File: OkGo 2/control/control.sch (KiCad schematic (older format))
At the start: 51 parts, among them P101 KEYSW, P102 KEYSW, P103 BATT_CASE, P104 BATT, P105 BATT, P106 ARM_LED, P107 ARM_LED, P108 SMA, P109 POWER_SW, P110 POWER_SW, SW101 KEYSWITCH, SW102 LATCHING PUSH, U101 SWD, U102 STM32F071CBT6, U103 MEJ2S0305SC, U104 BEZEL, U105 RFM95W, U106 LCD_HD44780, U107 ADP3335, Y101 8MHz

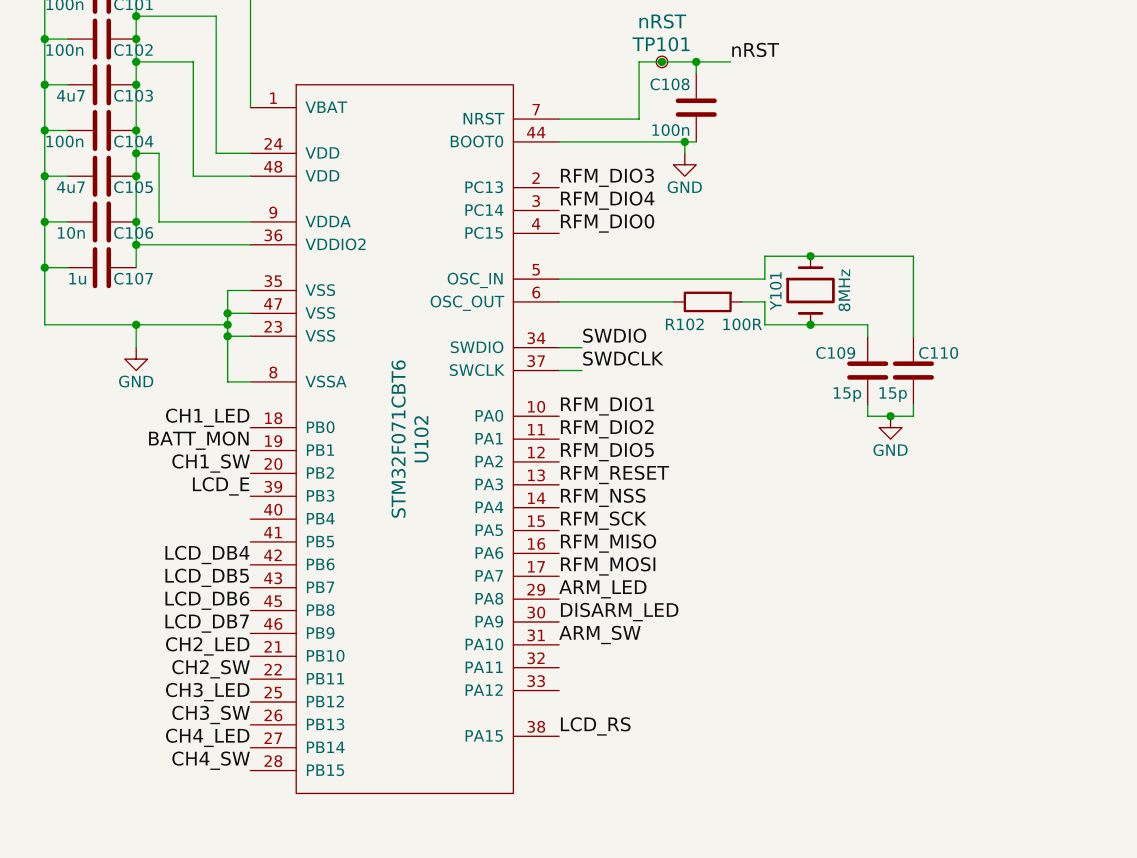
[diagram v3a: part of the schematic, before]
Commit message: Added serial interface, resolves #19
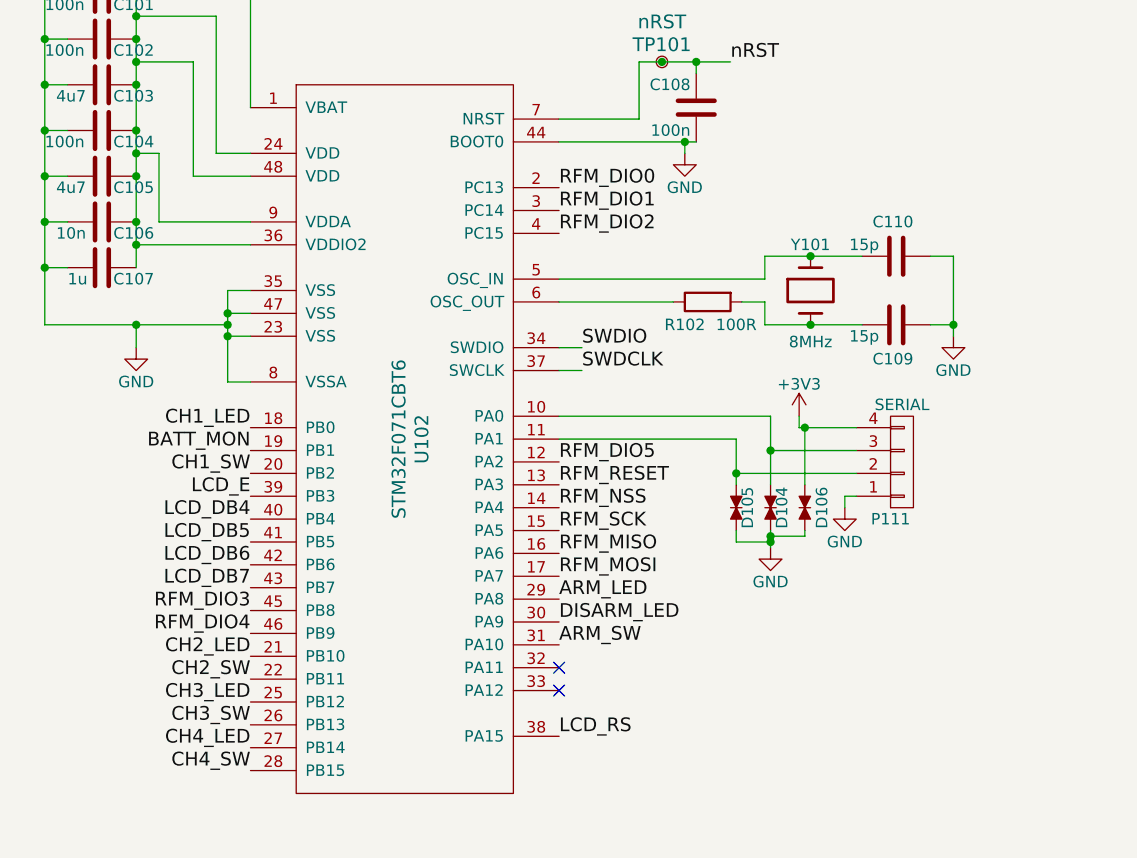
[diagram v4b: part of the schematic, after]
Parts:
- added D104, D105, D106: TVS_small, Resistors_SMD:R_0603, symbol TVS_small
- added P111: SERIAL, common:JST-PA-4, symbol CONN_01X04
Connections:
- net +3V3: now also D106.1, P111.4 (P4)
- net GND: now also D104.2, D105.2, D106.2, P111.1 (P1)
- net LCD_DB4: now also U102.40 (PB4); no longer U102.42 (PB6)
- net LCD_DB5: now also U102.41 (PB5); no longer U102.43 (PB7)
- net LCD_DB6: now also U102.42 (PB6); no longer U102.45 (PB8)
- net LCD_DB7: now also U102.43 (PB7); no longer U102.46 (PB9)
- net RFM_DIO0: now also U102.2 (PC13); no longer U102.4 (PC15)
- net RFM_DIO1: now also U102.3 (PC14); no longer U102.10 (PA0)
- net RFM_DIO2: now also U102.4 (PC15); no longer U102.11 (PA1)
- net RFM_DIO3: now also U102.45 (PB8); no longer U102.2 (PC13)
- net RFM_DIO4: now also U102.46 (PB9); no longer U102.3 (PC14)
- new net: D104.1, P111.3 (P3), U102.10 (PA0)
- new net: D105.1, P111.2 (P2), U102.11 (PA1)
- no-connect marks 2 -> 4
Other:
- moved on the sheet: C109, C110

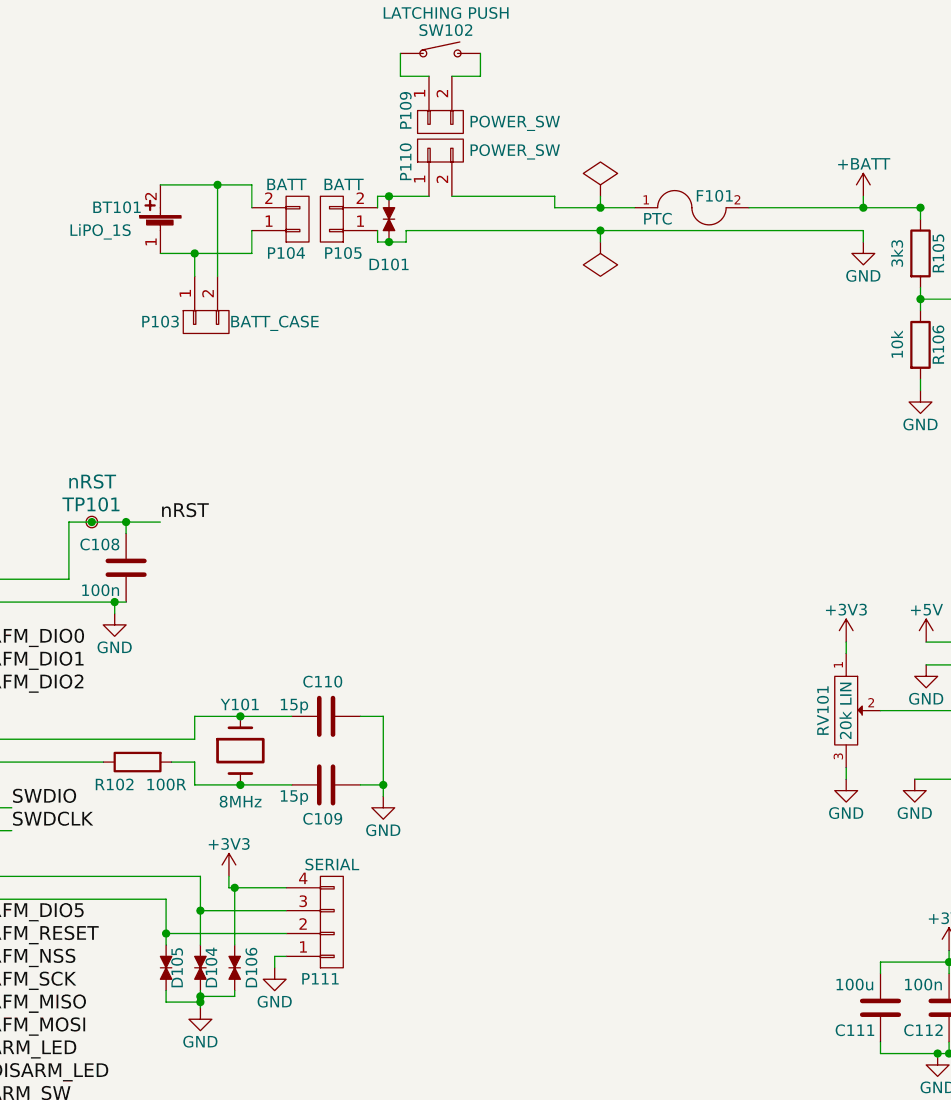
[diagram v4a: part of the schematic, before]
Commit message: 2nd route of control, sans cleaning and checking
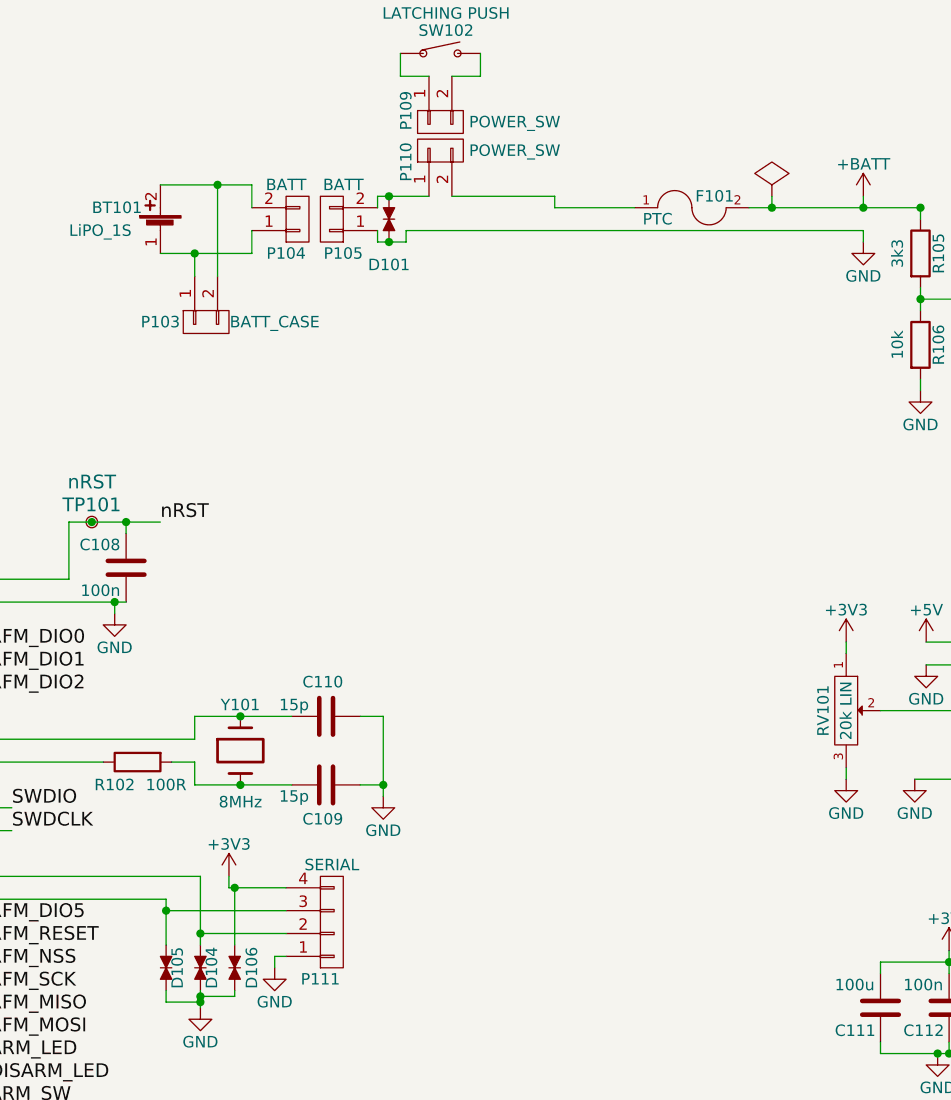
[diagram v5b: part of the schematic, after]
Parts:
- R106: footprint Capacitors_SMD:C_0805 -> Resistors_SMD:R_0805
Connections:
- net at D104.1, U102.10 (PA0): now also P111.2 (P2); no longer P111.3 (P3)
- net at D105.1, U102.11 (PA1): now also P111.3 (P3); no longer P111.2 (P2)
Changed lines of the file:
@@
 L PWR_FLAG #FLG06
 U 1 1 556217FC
-P 5725 1600
-F 0 "#FLG06" H 5725 1695 50  0001 C CNN
-F 1 "PWR_FLAG" H 5725 1780 50  0001 C CNN
-F 2 "" H 5725 1600 60  0000 C CNN
-F 3 "" H 5725 1600 60  0000 C CNN
-	1    5725 1600
-	1    0    0    -1
-$EndComp
-$Comp
-L PWR_FLAG #FLG07
-U 1 1 55621881
-P 5725 1800
-F 0 "#FLG07" H 5725 1895 50  0001 C CNN
-F 1 "PWR_FLAG" H 5725 1980 50  0001 C CNN
-F 2 "" H 5725 1800 60  0000 C CNN
-F 3 "" H 5725 1800 60  0000 C CNN
-	1    5725 1800
-	-1   0    0    1
-$EndComp
-$Comp
-L GND #PWR08
+P 6475 1600
+F 0 "#FLG06" H 6475 1695 50  0001 C CNN
+F 1 "PWR_FLAG" H 6475 1780 50  0001 C CNN
+F 2 "" H 6475 1600 60  0000 C CNN
+F 3 "" H 6475 1600 60  0000 C CNN
+	1    6475 1600
+	1    0    0    -1
+$EndComp
+$Comp
+L GND #PWR07
 U 1 1 55629E65
 P 9000 6300
-F 0 "#PWR08" H 9000 6050 50  0001 C CNN
+F 0 "#PWR07" H 9000 6050 50  0001 C CNN
 F 1 "GND" H 9000 6150 50  0001 C CNN
 F 2 "" H 9000 6300 60  0000 C CNN
@@
 $EndComp
 $Comp
-L GND #PWR09
+L GND #PWR08
 U 1 1 5562B214
 P 7200 5350
-F 0 "#PWR09" H 7200 5100 50  0001 C CNN
+F 0 "#PWR08" H 7200 5100 50  0001 C CNN
 F 1 "GND" H 7200 5200 50  0000 C CNN
 F 2 "" H 7200 5350 60  0000 C CNN
@@
 $EndComp
 $Comp
-L +3V3 #PWR010
+L +3V3 #PWR09
 U 1 1 5562B35A
 P 7250 4900
-F 0 "#PWR010" H 7250 4750 50  0001 C CNN
+F 0 "#PWR09" H 7250 4750 50  0001 C CNN
 F 1 "+3V3" H 7250 5040 50  0000 C CNN
 F 2 "" H 7250 4900 60  0000 C CNN
@@
 $EndComp
 $Comp
-L +3V3 #PWR011
+L +3V3 #PWR010
 U 1 1 55624CAA
 P 10650 850
-F 0 "#PWR011" H 10650 700 50  0001 C CNN
+F 0 "#PWR010" H 10650 700 50  0001 C CNN
 F 1 "+3V3" H 10650 990 50  0000 C CNN
 F 2 "" H 10650 850 60  0000 C CNN
@@
 $EndComp
 $Comp
-L +3V3 #PWR012
+L +3V3 #PWR011
 U 1 1 5562C6B7
 P 1200 2575
-F 0 "#PWR012" H 1200 2425 50  0001 C CNN
+F 0 "#PWR011" H 1200 2425 50  0001 C CNN
 F 1 "+3V3" H 1200 2715 50  0000 C CNN
 F 2 "" H 1200 2575 60  0000 C CNN
@@
 $EndComp
 $Comp
-L GND #PWR013
+L GND #PWR012
 U 1 1 5562DCAE
 P 1200 4275
-F 0 "#PWR013" H 1200 4025 50  0001 C CNN
+F 0 "#PWR012" H 1200 4025 50  0001 C CNN
 F 1 "GND" H 1200 4125 50  0000 C CNN
 F 2 "" H 1200 4275 60  0000 C CNN
@@
 $EndComp
 $Comp
-L GND #PWR014
+L GND #PWR013
 U 1 1 5562E73A
 P 3600 3425
-F 0 "#PWR014" H 3600 3175 50  0001 C CNN
+F 0 "#PWR013" H 3600 3175 50  0001 C CNN
 F 1 "GND" H 3600 3275 50  0000 C CNN
 F 2 "" H 3600 3425 60  0000 C CNN
@@
 $EndComp
 $Comp
-L +3V3 #PWR015
+L +3V3 #PWR014
 U 1 1 556484DA
 P 925 6750
-F 0 "#PWR015" H 925 6600 50  0001 C CNN
+F 0 "#PWR014" H 925 6600 50  0001 C CNN
 F 1 "+3V3" H 925 6890 50  0000 C CNN
 F 2 "" H 925 6750 60  0000 C CNN
@@
 $EndComp
 $Comp
-L GND #PWR016
+L GND #PWR015
 U 1 1 5564860C
 P 875 7250
-F 0 "#PWR016" H 875 7000 50  0001 C CNN
+F 0 "#PWR015" H 875 7000 50  0001 C CNN
 F 1 "GND" H 875 7100 50  0000 C CNN
 F 2 "" H 875 7250 60  0000 C CNN
@@
 F 0 "R106" V 7205 2250 50  0000 C CNN
 F 1 "10k" V 7025 2250 50  0000 C CNN
-F 2 "Capacitors_SMD:C_0805" V 7055 2250 30  0001 C CNN
+F 2 "Resistors_SMD:R_0805" V 7055 2250 30  0001 C CNN
 F 3 "" H 7125 2250 30  0000 C CNN
 F 4 "9237755" H 7125 2250 60  0001 C CNN "Farnell"
@@
 $EndComp
 $Comp
-L GND #PWR017
+L GND #PWR016
 U 1 1 556523AF
 P 7125 2450
-F 0 "#PWR017" H 7125 2200 50  0001 C CNN
+F 0 "#PWR016" H 7125 2200 50  0001 C CNN
 F 1 "GND" H 7125 2300 50  0000 C CNN
 F 2 "" H 7125 2450 60  0000 C CNN
@@
 $EndComp
 $Comp
-L +3V3 #PWR018
+L +3V3 #PWR017
 U 1 1 5563E071
 P 7500 3250
-F 0 "#PWR018" H 7500 3100 50  0001 C CNN
+F 0 "#PWR017" H 7500 3100 50  0001 C CNN
 F 1 "+3V3" H 7500 3390 50  0000 C CNN
 F 2 "" H 7500 3250 60  0000 C CNN
@@
 $EndComp
 $Comp
-L GND #PWR019
+L GND #PWR018
 U 1 1 5563E174
 P 7500 3350
-F 0 "#PWR019" H 7500 3100 50  0001 C CNN
+F 0 "#PWR018" H 7500 3100 50  0001 C CNN
 F 1 "GND" H 7500 3200 50  0000 C CNN
 F 2 "" H 7500 3350 60  0000 C CNN
@@
 $EndComp
 $Comp
-L +3V3 #PWR020
+L +3V3 #PWR019
 U 1 1 5563E7A7
 P 6800 3550
-F 0 "#PWR020" H 6800 3400 50  0001 C CNN
+F 0 "#PWR019" H 6800 3400 50  0001 C CNN
 F 1 "+3V3" H 6800 3690 50  0000 C CNN
 F 2 "" H 6800 3550 60  0000 C CNN
@@
 $EndComp
 $Comp
-L GND #PWR021
+L GND #PWR020
 U 1 1 5563E8D6
 P 6800 4150
-F 0 "#PWR021" H 6800 3900 50  0001 C CNN
+F 0 "#PWR020" H 6800 3900 50  0001 C CNN
 F 1 "GND" H 6800 4000 50  0000 C CNN
 F 2 "" H 6800 4150 60  0000 C CNN
@@
 $EndComp
 $Comp
-L GND #PWR022
+L GND #PWR021
 U 1 1 55643E77
 P 7150 3650
-F 0 "#PWR022" H 7150 3400 50  0001 C CNN
+F 0 "#PWR021" H 7150 3400 50  0001 C CNN
 F 1 "GND" H 7150 3500 50  0000 C CNN
 F 2 "" H 7150 3650 60  0000 C CNN
@@
 $EndComp
 $Comp
-L GND #PWR023
+L GND #PWR022
 U 1 1 55638AFF
 P 7100 4150
-F 0 "#PWR023" H 7100 3900 50  0001 C CNN
+F 0 "#PWR022" H 7100 3900 50  0001 C CNN
 F 1 "GND" H 7100 4000 50  0000 C CNN
 F 2 "" H 7100 4150 60  0000 C CNN
@@
 $EndComp
 $Comp
-L GND #PWR024
+L GND #PWR023
 U 1 1 559E503C
 P 9000 5850
-F 0 "#PWR024" H 9000 5600 50  0001 C CNN
+F 0 "#PWR023" H 9000 5600 50  0001 C CNN
 F 1 "GND" H 9000 5700 50  0001 C CNN
 F 2 "" H 9000 5850 60  0000 C CNN
@@
 $EndComp
 $Comp
-L +3V3 #PWR025
+L +3V3 #PWR024
 U 1 1 559EA6BB
 P 3150 7050
-F 0 "#PWR025" H 3150 6900 50  0001 C CNN
+F 0 "#PWR024" H 3150 6900 50  0001 C CNN
 F 1 "+3V3" H 3150 7190 50  0000 C CNN
 F 2 "" H 3150 7050 60  0000 C CNN
@@
 $EndComp
 $Comp
-L GND #PWR026
+L GND #PWR025
 U 1 1 559EA828
 P 3150 7250
-F 0 "#PWR026" H 3150 7000 50  0001 C CNN
+F 0 "#PWR025" H 3150 7000 50  0001 C CNN
 F 1 "GND" H 3150 7100 50  0000 C CNN
 F 2 "" H 3150 7250 60  0000 C CNN
@@
 $EndComp
 $Comp
-L +5V #PWR027
+L +5V #PWR026
 U 1 1 559EAA6F
 P 4350 7050
-F 0 "#PWR027" H 4350 6900 50  0001 C CNN
+F 0 "#PWR026" H 4350 6900 50  0001 C CNN
 F 1 "+5V" H 4350 7190 50  0000 C CNN
 F 2 "" H 4350 7050 60  0000 C CNN
@@
 $EndComp
 $Comp
-L GND #PWR028
+L GND #PWR027
 U 1 1 559EABE0
 P 4350 7250
-F 0 "#PWR028" H 4350 7000 50  0001 C CNN
+F 0 "#PWR027" H 4350 7000 50  0001 C CNN
 F 1 "GND" H 4350 7100 50  0000 C CNN
 F 2 "" H 4350 7250 60  0000 C CNN
@@
 $EndComp
 $Comp
-L +BATT #PWR029
+L +BATT #PWR028
 U 1 1 55A7EBCE
 P 8300 900
-F 0 "#PWR029" H 8300 750 50  0001 C CNN
+F 0 "#PWR028" H 8300 750 50  0001 C CNN
 F 1 "+BATT" H 8300 1040 50  0000 C CNN
 F 2 "" H 8300 900 60  0000 C CNN
@@
 $EndComp
 $Comp
-L GND #PWR030
+L GND #PWR029
 U 1 1 55A805A4
 P 10275 2750
-F 0 "#PWR030" H 10275 2500 50  0001 C CNN
+F 0 "#PWR029" H 10275 2500 50  0001 C CNN
 F 1 "GND" H 10275 2600 50  0000 C CNN
 F 2 "" H 10275 2750 60  0000 C CNN
@@
 $EndComp
 $Comp
-L +3.3V #PWR031
+L +3.3V #PWR030
 U 1 1 55A80891
 P 10325 2200
-F 0 "#PWR031" H 10325 2050 50  0001 C CNN
+F 0 "#PWR030" H 10325 2050 50  0001 C CNN
 F 1 "+3.3V" H 10325 2340 50  0000 C CNN
 F 2 "" H 10325 2200 60  0000 C CNN
@@
 GREEN: 2.1V 20mA
 $Comp
-L +5V #PWR032
+L +5V #PWR031
 U 1 1 55AC453D
 P 7150 3550
-F 0 "#PWR032" H 7150 3400 50  0001 C CNN
+F 0 "#PWR031" H 7150 3400 50  0001 C CNN
 F 1 "+5V" H 7150 3690 50  0000 C CNN
 F 2 "" H 7150 3550 60  0000 C CNN
@@
 $EndComp
 $Comp
-L GND #PWR033
+L GND #PWR032
 U 1 1 55B80248
 P 9400 4150
-F 0 "#PWR033" H 9400 3900 50  0001 C CNN
+F 0 "#PWR032" H 9400 3900 50  0001 C CNN
 F 1 "GND" H 9400 4000 50  0000 C CNN
 F 2 "" H 9400 4150 60  0000 C CNN
@@
 $EndComp
 $Comp
-L GND #PWR034
+L GND #PWR033
 U 1 1 55BA3B3F
 P 4775 4225
-F 0 "#PWR034" H 4775 3975 50  0001 C CNN
+F 0 "#PWR033" H 4775 3975 50  0001 C CNN
 F 1 "GND" H 4775 4075 50  0000 C CNN
 F 2 "" H 4775 4225 60  0000 C CNN
@@
 $EndComp
 $Comp
-L GND #PWR035
+L GND #PWR034
 U 1 1 55BA4EAC
 P 4300 4975
-F 0 "#PWR035" H 4300 4725 50  0001 C CNN
+F 0 "#PWR034" H 4300 4725 50  0001 C CNN
 F 1 "GND" H 4300 4825 50  0000 C CNN
 F 2 "" H 4300 4975 60  0000 C CNN
@@
 	4875 1750 6875 1750
 Wire Wire Line
-	5725 1600 5725 1650
-Connection ~ 5725 1650
-Wire Wire Line
-	5725 1800 5725 1750
-Connection ~ 5725 1750
-Wire Wire Line
 	6875 1650 6875 1600
 Wire Wire Line
@@
 	3050 4575 3975 4575
 $Comp
-L +3V3 #PWR036
+L +3V3 #PWR035
 U 1 1 55BB5B12
 P 4100 4575
-F 0 "#PWR036" H 4100 4425 50  0001 C CNN
+F 0 "#PWR035" H 4100 4425 50  0001 C CNN
 F 1 "+3V3" H 4100 4715 50  0000 C CNN
 F 2 "" H 4100 4575 60  0000 C CNN
@@
 	4300 4925 4300 4975
 Wire Wire Line
-	3975 4725 4350 4725
-Wire Wire Line
-	3825 4825 4350 4825
-Wire Wire Line
 	3975 4575 3975 4875
-Wire Wire Line
-	3825 4675 3825 4875
 Wire Wire Line
 	3825 4675 3050 4675
@@
 	4125 4625 4125 4875
 Connection ~ 4125 4625
-Connection ~ 3975 4725
-Connection ~ 3825 4825
-$Comp
-L GND #PWR037
+$Comp
+L GND #PWR036
 U 1 1 55BBFDE6
 P 3975 5150
-F 0 "#PWR037" H 3975 4900 50  0001 C CNN
+F 0 "#PWR036" H 3975 4900 50  0001 C CNN
 F 1 "GND" H 3975 5000 50  0000 C CNN
 F 2 "" H 3975 5150 60  0000 C CNN
@@
 NoConn ~ 3050 5675
 NoConn ~ 3050 5775
+Wire Wire Line
+	6475 1600 6475 1650
+Connection ~ 6475 1650
+Wire Wire Line
+	3825 4675 3825 4875
+Wire Wire Line
+	4350 4725 3825 4725
+Connection ~ 3825 4725
+Wire Wire Line
+	4350 4825 3975 4825
+Connection ~ 3975 4825
 $EndSCHEMATC

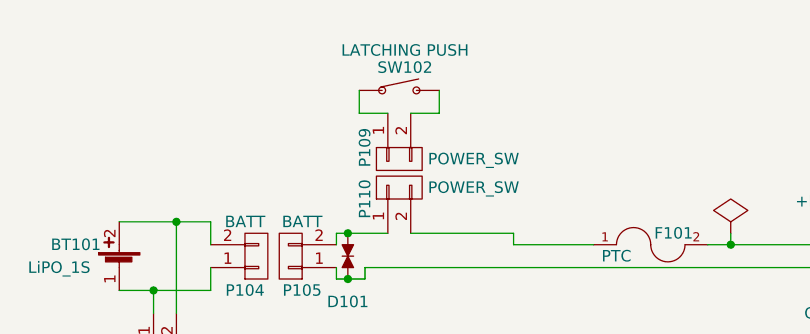
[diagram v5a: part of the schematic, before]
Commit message: Footprinting, rockers
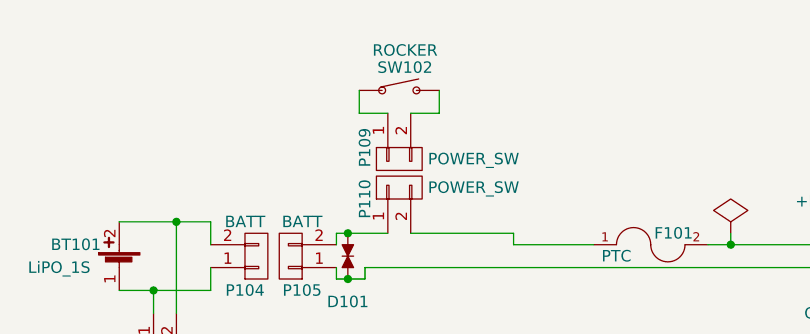
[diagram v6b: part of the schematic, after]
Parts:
- SW102: value LATCHING PUSH -> ROCKER; Farnell SW02719 -> 1839503
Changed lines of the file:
@@
 P 5050 975
 F 0 "SW102" H 5050 1075 50  0000 C CNN
-F 1 "LATCHING PUSH" H 5050 1150 50  0000 C CNN
+F 1 "ROCKER" H 5050 1150 50  0000 C CNN
 F 2 "" H 5050 975 60  0000 C CNN
-F 3 "" H 5050 975 60  0000 C CNN
-F 4 "SW02719" H 5050 975 60  0001 C CNN "Farnell"
+F 3 "http://www.farnell.com/datasheets/624901.pdf" H 5050 975 60  0001 C CNN
+F 4 "1839503" H 5050 975 60  0001 C CNN "Farnell"
 	1    5050 975
 	1    0    0    -1

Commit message: Changed SMA-F part
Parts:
- P108: Farnell 1608592 -> 1342651
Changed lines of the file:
@@
 F 2 "common:SMA-142-0701-801" H 9150 6050 60  0001 C CNN
 F 3 "" H 9150 6050 60  0000 C CNN
-F 4 "1608592" H 9150 6050 60  0001 C CNN "Farnell"
+F 4 "1342651" H 9150 6050 60  0001 C CNN "Farnell"
 	1    9150 6050
 	1    0    0    -1

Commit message: Corrected a bunch of footprints, see #9
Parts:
- F101: footprint Resistors_SMD:R_0805 -> control:polyfuse0805
- U102: footprint Housings_QFP:LQFP-48_7x7mm_Pitch0.5mm -> common:LQFP48_ST
- U107: footprint Housings_SSOP:MSOP-8_3x3mm_Pitch0.65mm -> control:MSOP-8_3x3mm_Pitch0.65mm
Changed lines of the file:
@@
 F 0 "U102" V 2450 4975 60  0000 C CNN
 F 1 "STM32F071CBT6" V 2350 4975 60  0000 C CNN
-F 2 "Housings_QFP:LQFP-48_7x7mm_Pitch0.5mm" H 2400 5025 60  0001 C CNN
+F 2 "common:LQFP48_ST" H 2400 5025 60  0001 C CNN
 F 3 "http://www.st.com/st-web-ui/static/active/en/resource/technical/document/datasheet/DM00098745.pdf" H 2400 5025 60  0001 C CNN
 F 4 "2432093" H 2400 4825 60  0001 C CNN "Farnell"
@@
 F 0 "U107" V 9500 950 60  0000 C CNN
 F 1 "ADP3335" V 9400 950 60  0000 C CNN
-F 2 "Housings_SSOP:MSOP-8_3x3mm_Pitch0.65mm" H 9400 1100 60  0001 C CNN
+F 2 "control:MSOP-8_3x3mm_Pitch0.65mm" H 9400 1100 60  0001 C CNN
 F 3 "" H 9400 1100 60  0000 C CNN
 F 4 "2067775" H 9400 950 60  0001 C CNN "Farnell"
@@
 F 0 "F101" H 6225 1700 50  0000 C CNN
 F 1 "PTC" H 5975 1600 50  0000 C CNN
-F 2 "Resistors_SMD:R_0805" H 6125 1650 60  0001 C CNN
+F 2 "control:polyfuse0805" H 6125 1650 60  0001 C CNN
 F 3 "" H 6125 1650 60  0000 C CNN
 F 4 "1294879" H 6125 1650 60  0001 C CNN "Farnell"
